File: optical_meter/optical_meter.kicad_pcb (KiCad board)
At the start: 2 copper layers, 50 parts, among them J1 SFP+, J2 SFP+, J3 Conn_01x02_Pin, J4 Conn_02x03, U2 FIN1002M5X, U3 FIN1001M5X, U4 Pico

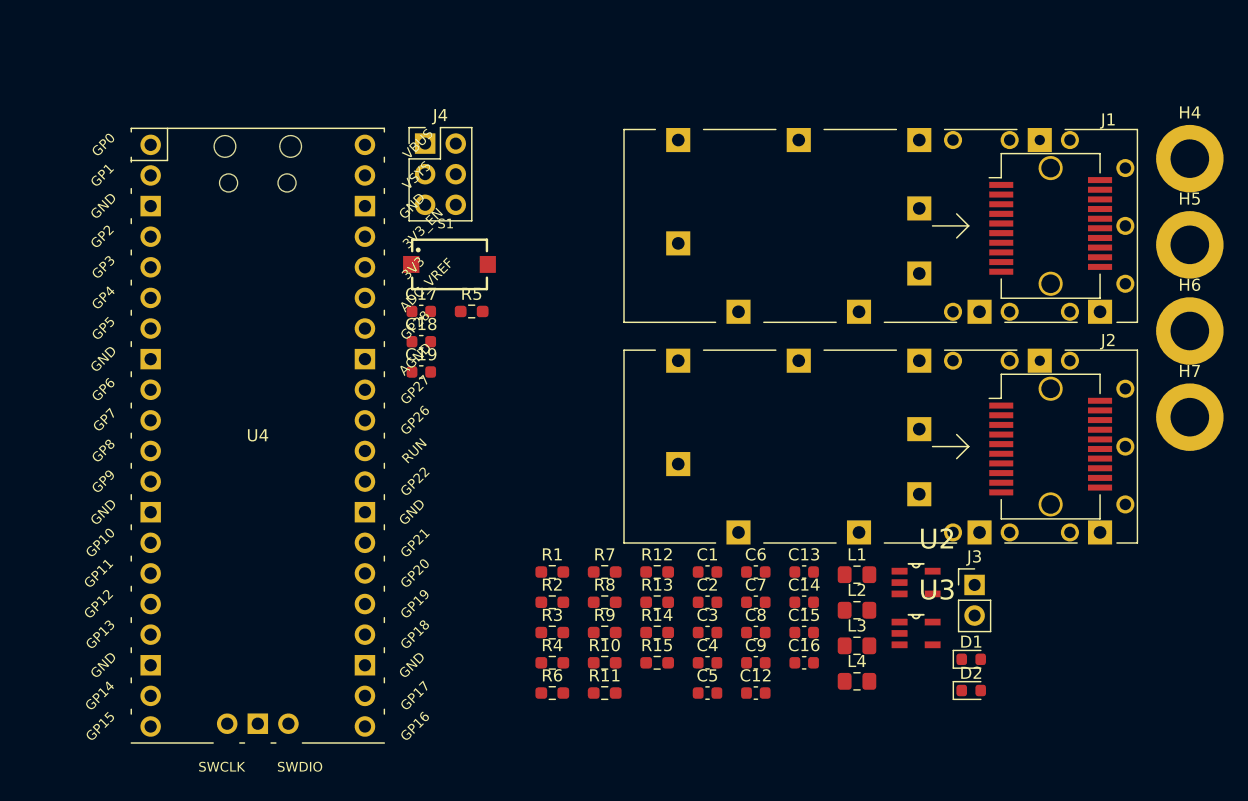
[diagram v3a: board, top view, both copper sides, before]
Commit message: Fixing some 3D model file paths
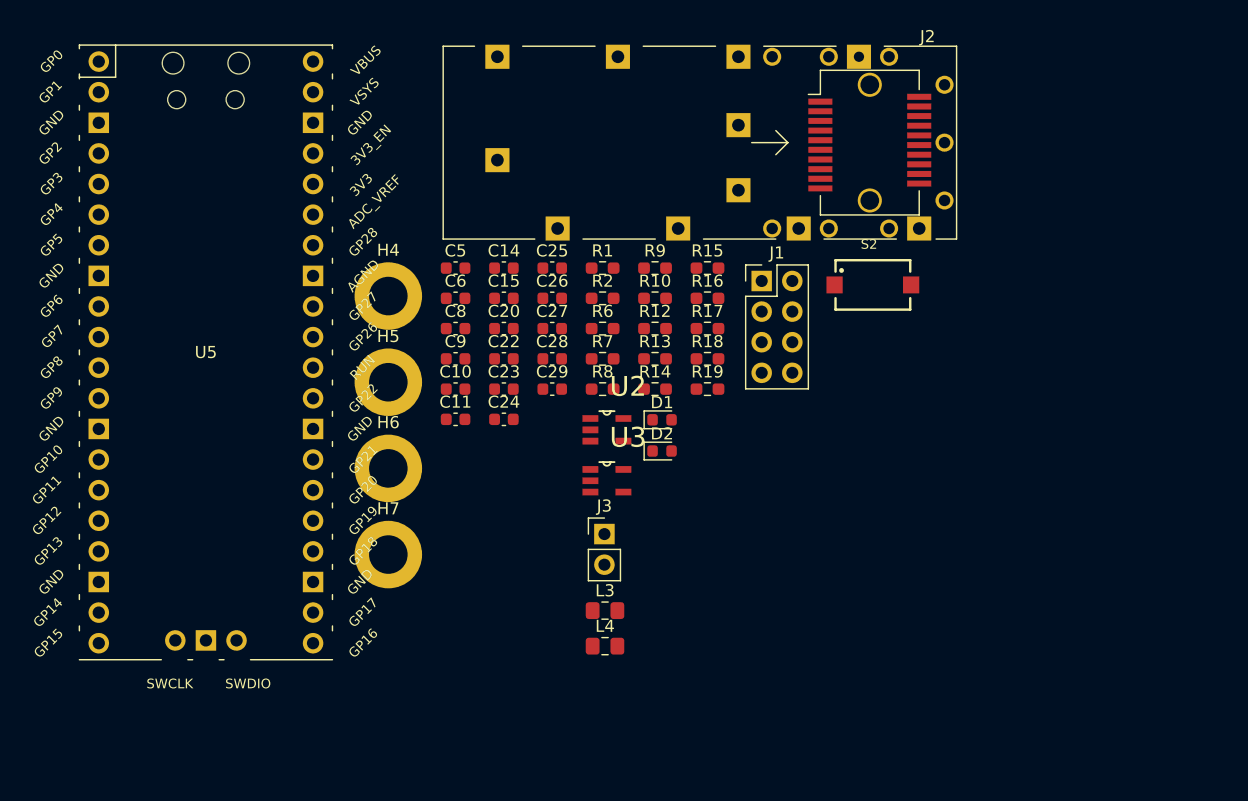
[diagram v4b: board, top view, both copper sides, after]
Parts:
- removed C1, C16, C18, C19, C7: 4u7, Capacitor_SMD:C_0603_1608Metric
- removed C12, C13, C17, C2, C3, C4: 100n, Capacitor_SMD:C_0603_1608Metric
- removed J4: Conn_02x03, Connector_PinHeader_2.54mm:PinHeader_2x03_P2.54mm_Vertical
- removed L1, L2: 1u, Inductor_SMD:L_0805_2012Metric_Pad1.15x1.40mm_HandSolder
- removed R11, R3, R4, R5: 4k7, Resistor_SMD:R_0603_1608Metric_Pad0.98x0.95mm_HandSolder
- removed S1: SW Push, SW_Push:434123025816
- removed U4: Pico, MCU_RaspberryPi_and_Boards:RPi_Pico_SMD_TH
- added C10: 2u2, Capacitor_SMD:C_0603_1608Metric, F.Cu at (205.6, 57.2)
- added C11: 100n, Capacitor_SMD:C_0603_1608Metric, F.Cu at (205.6, 59.7)
- added C20: 2u2, Capacitor_SMD:C_0603_1608Metric, F.Cu at (209.6, 52.1)
- added C22: 100n, Capacitor_SMD:C_0603_1608Metric, F.Cu at (209.6, 54.7)
- added C23: 100n, Capacitor_SMD:C_0603_1608Metric, F.Cu at (209.6, 57.2)
- added C24: 100n, Capacitor_SMD:C_0603_1608Metric, F.Cu at (209.6, 59.7)
- added C25: 100n, Capacitor_SMD:C_0603_1608Metric, F.Cu at (213.6, 47.1)
- added C26: 100n, Capacitor_SMD:C_0603_1608Metric, F.Cu at (213.6, 49.6)
- added C27: 2u2, Capacitor_SMD:C_0603_1608Metric, F.Cu at (213.6, 52.1)
- added C28: 100n, Capacitor_SMD:C_0603_1608Metric, F.Cu at (213.6, 54.7)
- added C29: 100n, Capacitor_SMD:C_0603_1608Metric, F.Cu at (213.6, 57.2)
- added R16: 137R, Resistor_SMD:R_0603_1608Metric_Pad0.98x0.95mm_HandSolder, F.Cu at (226.5, 49.6)
- added R17: 78R, Resistor_SMD:R_0603_1608Metric_Pad0.98x0.95mm_HandSolder, F.Cu at (226.5, 52.1)
- added R18: 137R, Resistor_SMD:R_0603_1608Metric_Pad0.98x0.95mm_HandSolder, F.Cu at (226.5, 54.7)
- added R19: 78R, Resistor_SMD:R_0603_1608Metric_Pad0.98x0.95mm_HandSolder, F.Cu at (226.5, 57.2)
- added S2: SW Push, SW_Push:434123025816, F.Cu at (240.2, 48.5)
- added U5: Pico, MCU_RaspberryPi_and_Boards:RPi_Pico_SMD_TH, F.Cu at (184.9, 54.1)
- J1: value SFP+ -> Conn_02x04; footprint SFP:Connector_SFP_and_Cage -> Connector_PinHeader_2.54mm:PinHeader_2x04_P2.54mm_Vertical
- R10: value 100 -> 4k7
- R9: value 100 -> 0R
- moved H4 67.5 mm to (200.0, 49.5)
- moved H7 67.5 mm to (200.0, 70.9)
- moved H5 67.5 mm to (200.0, 56.6)
- moved H6 67.5 mm to (200.0, 63.8)
- moved C5 41.0 mm to (205.6, 47.1)
- moved C15 37.3 mm to (209.6, 49.6)
- moved C14 37.3 mm to (209.6, 47.1)
- moved C8 35.5 mm to (205.6, 52.1)
- moved C9 35.5 mm to (205.6, 54.7)
- moved C6 33.7 mm to (205.6, 49.6)
- moved R15 33.0 mm to (226.5, 47.1)
- moved D1 32.4 mm to (222.7, 59.7)
- moved D2 32.4 mm to (222.7, 62.3)
- moved J3 31.0 mm to (217.9, 69.2)
- moved R6 30.5 mm to (217.8, 52.1)
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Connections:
- net /RX_LOS1 renamed /RX_LOS
- net /TX_FAULT1 renamed /TX_FAULT
- C14 pad 1: GND -> +3V3
- C15 pad 2: GND -> +3V3
- C5 pad 1: GND -> +3V3
- C6 pad 1: GND -> +3V3
- C8 pad 2: GND -> +3V3
- C9 pad 1: GND -> +3V3
- H4 pad 1: GND -> +3V3
- H5 pad 1: GND -> +3V3
- H6 pad 1: GND -> +3V3
- H7 pad 1: GND -> +3V3
- J1 pad 1: GND -> /GPIO17
- J1 pad 2: /TX_FAULT0 -> /GPIO16
- J1 pad 3: /TX_DISABLE0 -> +3V3
- J1 pad 4: /SDA0 -> +5V
- J1 pad 5: /SCL0 -> +3V3
- J1 pad 6: GND -> +3V3
- J1 pad 7: /RS00 -> /GPIO14
- J1 pad 8: /RX_LOS0 -> /GPIO15
- J2 pad 1: GND -> +3V3
- J2 pad 10: GND -> +3V3
- J2 pad 11: GND -> +3V3
- J2 pad 12: /RD1- -> Net-(J2-RD-)
- J2 pad 13: /RD1+ -> Net-(J2-RD+)
- J2 pad 14: GND -> +3V3
- J2 pad 17: GND -> +3V3
- J2 pad 18: unconnected-(J2-TD+-Pad18) -> /TD+
- J2 pad 19: unconnected-(J2-TD--Pad19) -> /TD-
- J2 pad 20: GND -> +3V3
- J2 pad 3: /TX_DISABLE1 -> /TX_DISABLE
- J2 pad 4: /SDA1 -> /SDA
- J2 pad 5: /SCL1 -> /SCL
- J2 pad 6: GND -> Net-(J2-MOD_ABS)
- J2 pad 7: /RS01 -> /RS0
- J2 pad 9: /RS11 -> /RS1
- J2 pad CAGE: GND -> +3V3
- J3 pad 2: GND -> +3V3
- R1 pad 2: GND -> +3V3
- R10 pad 1: Net-(U2-RIN-) -> +3V3
- R10 pad 2: Net-(U2-RIN+) -> /RUN
- R12 pad 1: Net-(U2-RIN+) -> /RD+
- R13 pad 1: GND -> +3V3
- R13 pad 2: Net-(U2-RIN+) -> /RD+
- R14 pad 1: Net-(U2-RIN-) -> /RD-
- R15 pad 1: GND -> +3V3
- R15 pad 2: Net-(U2-RIN-) -> /RD-
- R2 pad 2: GND -> +3V3
- R6 pad 1: /TX_DISABLE1 -> +3V3
- R6 pad 2: +3V3 -> /TX_DISABLE
- R8 pad 1: unconnected-(R8-Pad1) -> +3V3
- R9 pad 1: /TD0+ -> Net-(J2-MOD_ABS)
- R9 pad 2: /TD0- -> +3V3
- U2 pad 2: GND -> +3V3
- U2 pad 3: Net-(U2-RIN+) -> /RD+
- U2 pad 4: Net-(U2-RIN-) -> /RD-
- U3 pad 2: GND -> +3V3
- U3 pad 3: /TD0- -> Net-(U3-DOUT-)
- U3 pad 4: /TD0+ -> Net-(U3-DOUT+)

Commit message: Defining PCB design rules. Adding net class for differential LVDSpairs with necessary calculations made
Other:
- copper layers 2 -> 4
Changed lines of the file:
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@@
 	(generator_version "9.0")
 	(general
-		(thickness 1.6)
+		(thickness 1.6062)
 		(legacy_teardrops no)
 	)
@@
 	(layers
 		(0 "F.Cu" signal)
+		(4 "In1.Cu" signal)
+		(6 "In2.Cu" signal)
 		(2 "B.Cu" signal)
 		(9 "F.Adhes" user "F.Adhesive")
@@
 	)
 	(setup
+		(stackup
+			(layer "F.SilkS"
+				(type "Top Silk Screen")
+			)
+			(layer "F.Paste"
+				(type "Top Solder Paste")
+			)
+			(layer "F.Mask"
+				(type "Top Solder Mask")
+				(thickness 0.01)
+			)
+			(layer "F.Cu"
+				(type "copper")
+				(thickness 0.035)
+			)
+			(layer "dielectric 1"
+				(type "prepreg")
+				(thickness 0.2104)
+				(material "FR4")
+				(epsilon_r 4.5)
+				(loss_tangent 0.02)
+			)
+			(layer "In1.Cu"
+				(type "copper")
+				(thickness 0.0152)
+			)
+			(layer "dielectric 2"
+				(type "core")
+				(thickness 1.065)
+				(material "FR4")
+				(epsilon_r 4.5)
+				(loss_tangent 0.02)
+			)
+			(layer "In2.Cu"
+				(type "copper")
+				(thickness 0.0152)
+			)
+			(layer "dielectric 3"
+				(type "prepreg")
+				(thickness 0.2104)
+				(material "FR4")
+				(epsilon_r 4.5)
+				(loss_tangent 0.02)
+			)
+			(layer "B.Cu"
+				(type "copper")
+				(thickness 0.035)
+			)
+			(layer "B.Mask"
+				(type "Bottom Solder Mask")
+				(thickness 0.01)
+			)
+			(layer "B.Paste"
+				(type "Bottom Solder Paste")
+			)
+			(layer "B.SilkS"
+				(type "Bottom Silk Screen")
+			)
+			(copper_finish "None")
+			(dielectric_constraints yes)
+		)
 		(pad_to_mask_clearance 0)
 		(allow_soldermask_bridges_in_footprints no)

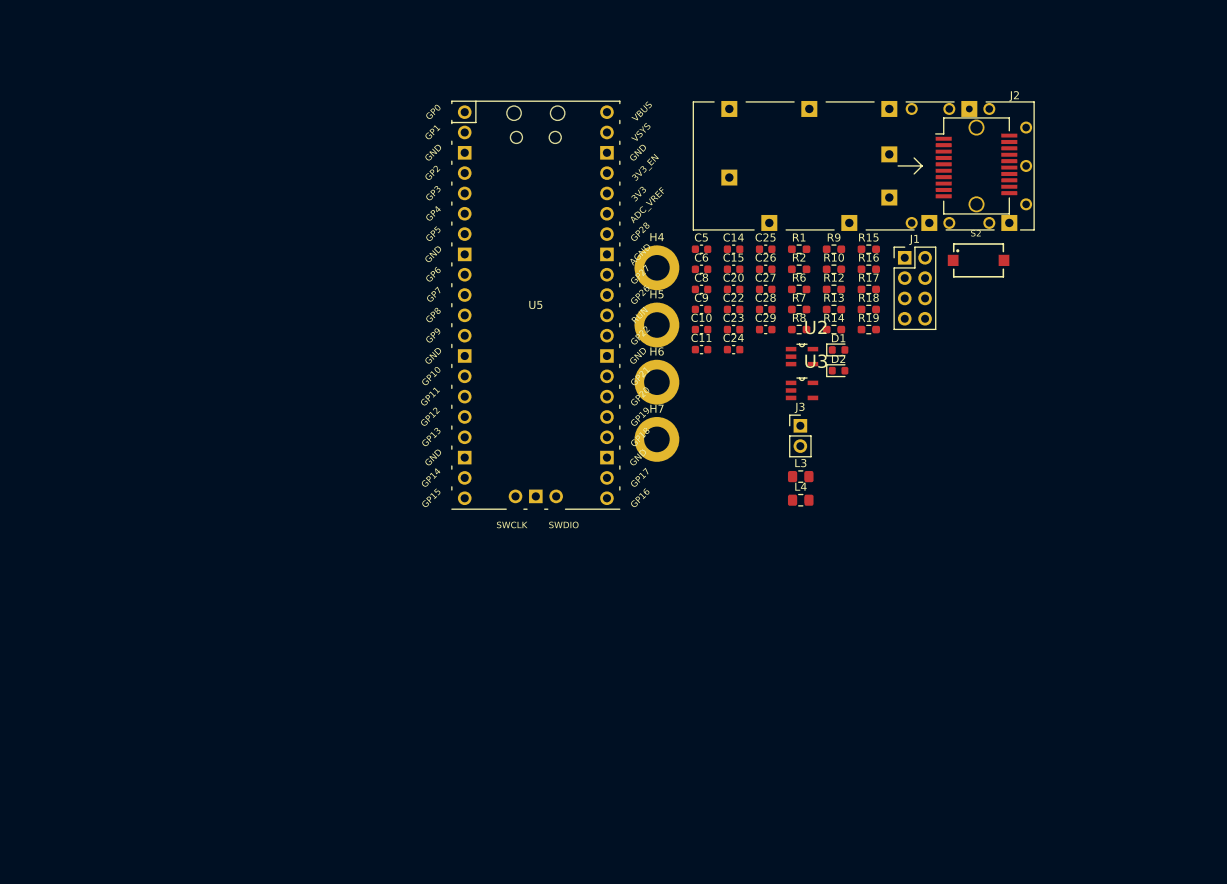
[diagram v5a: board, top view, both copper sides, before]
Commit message: fixing accidental short of GND to 3v3
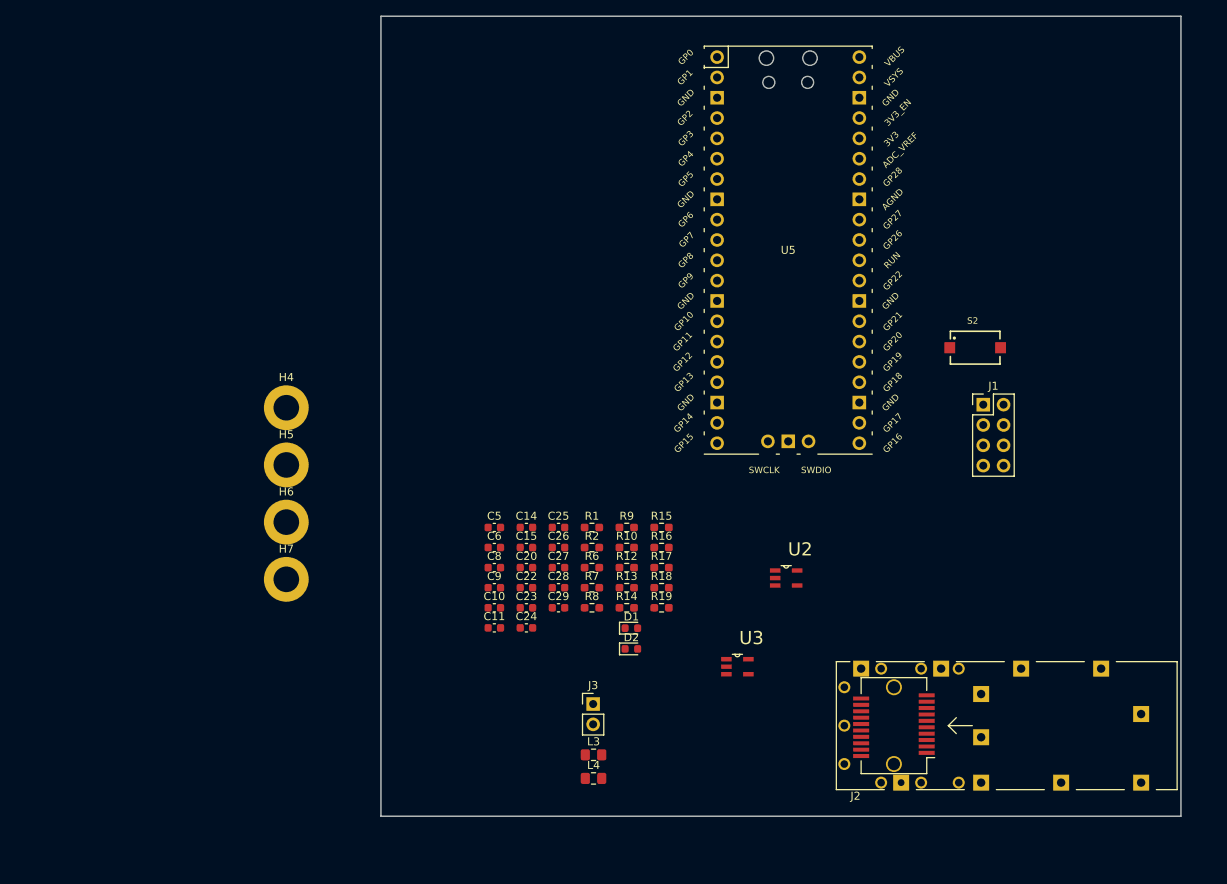
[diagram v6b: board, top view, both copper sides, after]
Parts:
- U2: value FIN1002M5X -> LVDS -> LVTTL
- U3: value FIN1001M5X -> LVTTL -> LVDS
- moved J2 73.6 mm to (223.4, 106.7), turned to 180 degrees
- moved H5 49.5 mm to (153.7, 74.1)
- moved H6 49.5 mm to (153.7, 81.2)
- moved H4 49.5 mm to (153.7, 66.9)
- moved H7 49.5 mm to (153.7, 88.4)
- moved C15 43.4 mm to (183.7, 84.4)
- moved C22 43.4 mm to (183.7, 89.4)
- moved C26 43.4 mm to (187.7, 84.4)
- moved C28 43.4 mm to (187.7, 89.4)
- moved C6 43.4 mm to (179.7, 84.4)
- moved C9 43.4 mm to (179.7, 89.4)
- moved D1 43.4 mm to (196.8, 94.5)
- moved L3 43.4 mm to (192.1, 110.3)
- moved L4 43.4 mm to (192.1, 113.3)
- moved R10 43.4 mm to (196.2, 84.4)
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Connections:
- net Net-(J2-RD+) renamed /SFP_RD+
- net Net-(J2-RD-) renamed /SFP_RD-
- net Net-(U3-DOUT+) renamed /U3_TD+
- net Net-(U3-DOUT-) renamed /U3_TD-
- C10 pad 1: +3V3 -> GND
- C11 pad 1: +3V3 -> GND
- C14 pad 2: +3V3 -> GND
- C15 pad 2: +3V3 -> GND
- C20 pad 1: +3V3 -> GND
- C24 pad 2: +3V3 -> GND
- C25 pad 1: +3V3 -> GND
- C27 pad 2: +3V3 -> GND
- C28 pad 2: +3V3 -> GND
- C5 pad 1: +3V3 -> GND
- C6 pad 1: +3V3 -> GND
- C8 pad 2: +3V3 -> GND
- C9 pad 1: +3V3 -> GND
- H4 pad 1: +3V3 -> GND
- H5 pad 1: +3V3 -> GND
- H6 pad 1: +3V3 -> GND
- H7 pad 1: +3V3 -> GND
- J1 pad 5: +3V3 -> GND
- J1 pad 6: +3V3 -> GND
- J2 pad 1: +3V3 -> GND
- J2 pad 10: +3V3 -> GND
- J2 pad 11: +3V3 -> GND
- J2 pad 14: +3V3 -> GND
- J2 pad 17: +3V3 -> GND
- J2 pad 20: +3V3 -> GND
- J2 pad CAGE: +3V3 -> GND
- J3 pad 2: +3V3 -> GND
- R1 pad 2: +3V3 -> GND
- R13 pad 1: +3V3 -> GND
- R15 pad 1: +3V3 -> GND
- R17 pad 1: +3V3 -> GND
- R19 pad 1: +3V3 -> GND
- R2 pad 2: +3V3 -> GND
- R9 pad 2: +3V3 -> GND
- S2 pad 2: +3V3 -> GND
- U2 pad 2: +3V3 -> GND
- U3 pad 2: +3V3 -> GND
- U5 pad 13: +3V3 -> GND
- U5 pad 18: +3V3 -> GND
- U5 pad 23: +3V3 -> GND
- U5 pad 28: +3V3 -> GND
- U5 pad 3: +3V3 -> GND
- U5 pad 33: +3V3 -> GND
- U5 pad 38: +3V3 -> GND
- U5 pad 42: +3V3 -> GND
- U5 pad 8: +3V3 -> GND
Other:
- board outline added: 100 x 100 mm
